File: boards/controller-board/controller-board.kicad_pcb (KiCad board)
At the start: 2 copper layers, 130 x 115 mm, 178 parts, among them J1 Conn_01x02, J2 Conn_01x02, J3 Conn_01x02, J4 Conn_01x02, J5 Conn_01x03, J6 Conn_01x02, Q1 SQS460EN, Q2 DGD0216, SW1 EG1271, U1 CAT4201, U10 CAT4201, U11 CAT4201, U12 CAT4201, U13 CAT4201, U14 CAT4201, U15 CAT4201, U17 CAT4201, U18 CAT4201, U2 PocketBeagle, U3 LTC3624, U4 CAT4201, U5 CAT4201, U6 CAT4201, U7 MCP4728, U8 ADS1015IRUGR, U9 ADS1015IRUGR

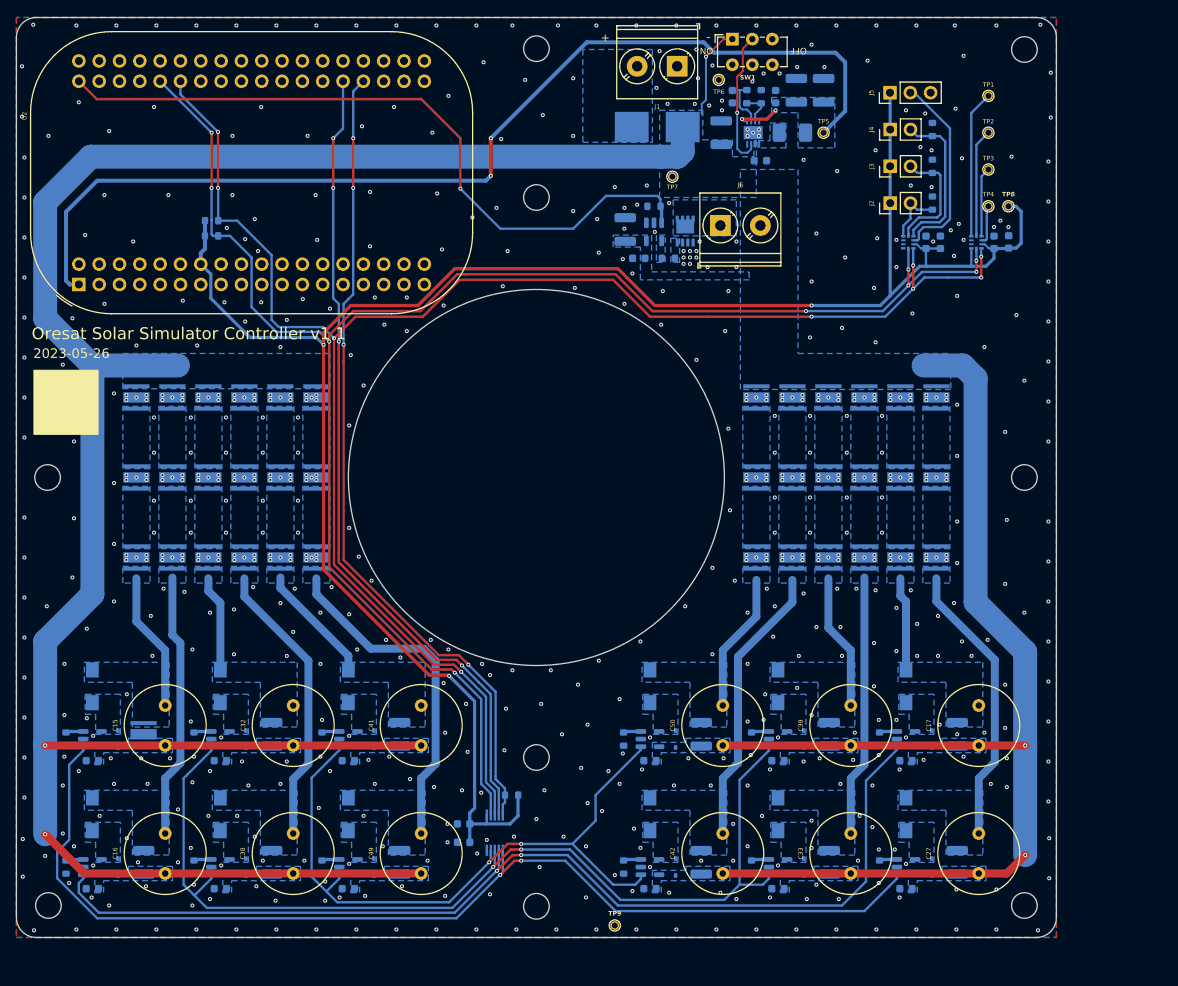
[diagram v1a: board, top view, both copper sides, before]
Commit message: moved LED driver circuitry to front layer of PCB
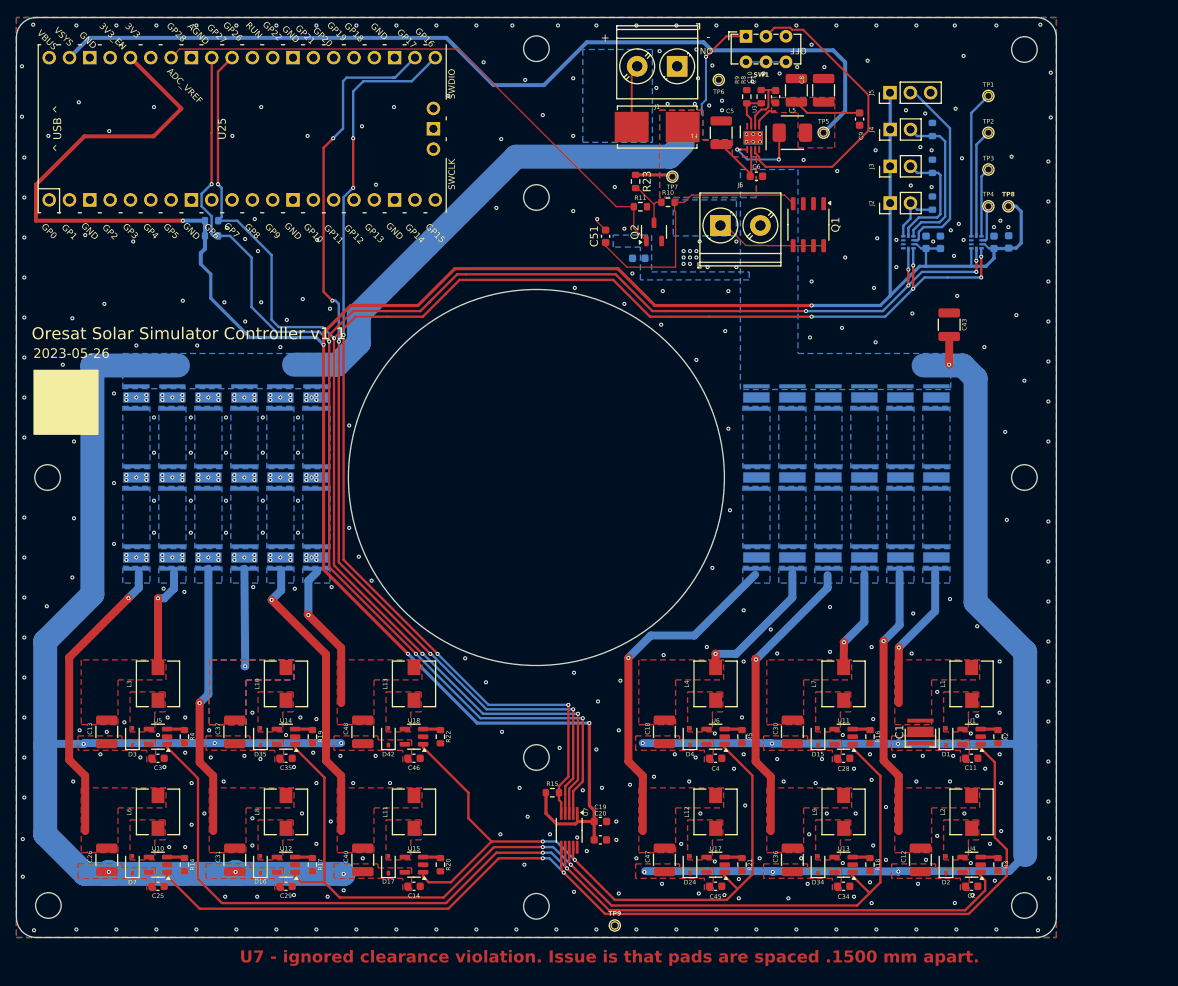
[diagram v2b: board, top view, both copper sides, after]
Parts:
- removed C15, C16, C17, C27, C32, C33, C38, C39, C41, C42, C49, C50: NP, Capacitor_THT:C_Radial_D10.0mm_H16.0mm_P5.00mm
- removed U2: PocketBeagle, Module:BeagleBoard_PocketBeagle
- added C51: C_Small, Capacitor_SMD:C_0603_1608Metric, F.Cu at (153.7, 72.3)
- added R23: 1k, Resistor_SMD:R_0603_1608Metric, F.Cu at (157.4, 65.5)
- added U25: RPi_Pico, oresat-misc:RPi_Pico_TH, F.Cu at (108.2, 58.9)
- C1, C10, C11, C12, C13, C14, C18, C19, C2, C20, C25, C26, C28, C29, C3, C30, C31, C34, C35, C36, C37, C4, C40, C43, C45, C46, C47, C48, C5, C6, C7, C8, C9, D1, D15, D16, D17, D2, D24, D3, D34, D35, D4, D42, D7, F1, L1, L10, L11, L12, L13, L2, L3, L4, L5, L6, L7, L8, L9, R10, R11, R14, R15, R16, R17, R18, R19, R2, R20, R21, R22, R3, R4, R5, R8, R9, U1, U10, U11, U12, U13, U14, U15, U17, U18, U4, U5, U6, U7: moved to F.Cu
- D18, D19, D20, D21: value XPEBBL-L1-0000-00201 -> ELUA3535OGB-P6070U23240500-VD1M
- D22, D23, D47, D48: value XPEBBL-L1-0000-00201 -> NP
- D43, D44, D45, D46: value XPEBBL-L1-0000-00201 -> ELUC3535NUB-P7085Q15070100-S22Q
- Q1: value SQS460EN -> Goford_G11S_20V_11A; footprint Package_SO:Vishay_PowerPAK_1212-8_Single -> Package_SO:SOP-8_3.9x4.9mm_P1.27mm; moved to F.Cu
- Q2: value DGD0216 -> PMV45EN; footprint Package_TO_SOT_SMD:TSOT-23-5 -> Package_TO_SOT_SMD:SOT-23-3; moved to F.Cu
- U3: footprint Package_DFN_QFN:DFN-8-1EP_3x3mm_P0.5mm_EP1.65x2.38mm -> oresat-ics:DFN-8-1EP_3x3mm_P0.5mm_EP1.65x2.38mm_ThermalVias0.3mm; moved to F.Cu
- moved R2 116.5 mm to (202.7, 134.9)
- moved R3 116.5 mm to (202.7, 150.9)
- moved C11 109.9 mm to (199.4, 137.6), turned to 0 degrees
- moved C2 109.9 mm to (199.4, 153.6), turned to 0 degrees
- moved L1 109.9 mm to (199.4, 128.3)
- moved L2 109.9 mm to (199.4, 144.3)
- moved U1 109.9 mm to (199.4, 134.9), turned to 180 degrees
- moved U4 109.9 mm to (199.4, 150.9), turned to 180 degrees
- moved C13 106.3 mm to (91.3, 134.3)
- moved C26 106.3 mm to (91.3, 150.3)
- moved D1 103.5 mm to (196.2, 134.9)
- moved D2 103.5 mm to (196.2, 150.9)
- moved D3 99.9 mm to (94.5, 134.9)
- moved D7 99.9 mm to (94.5, 150.9)
- moved C1 97.1 mm to (193.0, 134.3)
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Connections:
- C1 pad 2: Net-(D8-K) -> Net-(D26-K)
- C12 pad 2: Net-(D10-K) -> Net-(D12-K)
- C13 pad 2: Net-(D12-K) -> Net-(D10-K)
- C18 pad 2: Net-(D19-K) -> Net-(D21-K)
- C26 pad 2: Net-(D26-K) -> Net-(D8-K)
- C30 pad 2: Net-(D29-K) -> Net-(D31-K)
- C31 pad 2: Net-(D31-K) -> Net-(D29-K)
- C36 pad 2: Net-(D37-K) -> Net-(D39-K)
- C37 pad 2: Net-(D39-K) -> Net-(D37-K)
- C40 pad 2: Net-(D21-K) -> Net-(D19-K)
- C47 pad 2: Net-(D44-K) -> Net-(D46-K)
- C48 pad 2: Net-(D46-K) -> Net-(D44-K)
- L1 pad 2: Net-(D8-K) -> Net-(D26-K)
- L10 pad 2: Net-(D39-K) -> Net-(D37-K)
- L11 pad 2: Net-(D21-K) -> Net-(D19-K)
- L12 pad 2: Net-(D44-K) -> Net-(D46-K)
- L13 pad 2: Net-(D46-K) -> Net-(D44-K)
- L2 pad 2: Net-(D10-K) -> Net-(D12-K)
- L3 pad 2: Net-(D12-K) -> Net-(D10-K)
- L4 pad 2: Net-(D19-K) -> Net-(D21-K)
- L6 pad 2: Net-(D26-K) -> Net-(D8-K)
- L7 pad 2: Net-(D29-K) -> Net-(D31-K)
- L8 pad 2: Net-(D31-K) -> Net-(D29-K)
- L9 pad 2: Net-(D37-K) -> Net-(D39-K)
- Q2 pad 1: unconnected-(Q2-~{IN}-Pad1) -> Net-(Q2-G)
- Q2 pad 3: Net-(Q2-IN) -> Net-(Q2-D)
- R10 pad 1: Net-(Q2-OUT) -> Net-(Q2-D)
- R11 pad 1: Net-(Q2-IN) -> Net-(Q2-G)
- SW1 pad 4: (no net) -> GND
- SW1 pad 5: (no net) -> GND
- SW1 pad 6: (no net) -> GND
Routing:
- net Net-(Q2-IN): track 88.9 -> 0.00 mm, vias 1 -> 0
- net Net-(Q2-G): track 0.00 -> 71.9 mm
- net +3.3V: track 247.7 -> 317.2 mm, vias 3 -> 5
- net Net-(Q1-G): track 0.00 -> 34.1 mm
- net Net-(D46-K): track 17.4 -> 42.6 mm, vias 0 -> 1
- net Net-(D44-K): track 42.7 -> 18.7 mm, vias 0 -> 1
- net VCC: track 431.4 -> 407.6 mm, vias 5 -> 14
- net Net-(D37-K): track 36.0 -> 12.4 mm, vias 0 -> 1
- net Net-(D12-K): track 11.7 -> 33.9 mm, vias 0 -> 1
- net Net-(D29-K): track 12.1 -> 34.1 mm, vias 0 -> 1
- net Net-(D19-K): track 15.1 -> 36.5 mm, vias 0 -> 1
- net Net-(SW1-B): track 17.2 -> 38.6 mm, vias 1 -> 0
- net /DAC_~{LDAC}: track 102.3 -> 122.6 mm, vias 4 -> 5
- net Net-(D10-K): track 33.2 -> 13.2 mm, vias 0 -> 1
- net Net-(D31-K): track 32.7 -> 12.8 mm, vias 0 -> 1
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- added copper zone on F.Cu, net +5V
- added copper zone on F.Cu, net Net-(D1-A)
- added copper zone on F.Cu, net Net-(D10-K)
- added copper zone on F.Cu, net Net-(D12-K)
- added copper zone on F.Cu, net Net-(D15-A)
- added copper zone on F.Cu, net Net-(D16-A)
- added copper zone on F.Cu, net Net-(D17-A)
- added copper zone on F.Cu, net Net-(D19-K)
- added copper zone on F.Cu, net Net-(D2-A)
- added copper zone on F.Cu, net Net-(D21-K)
- added copper zone on F.Cu, net Net-(D24-A)
- added copper zone on F.Cu, net Net-(D26-K)
- added copper zone on F.Cu, net Net-(D29-K)
- added copper zone on F.Cu, net Net-(D3-A)
- added copper zone on F.Cu, net Net-(D31-K)
- added copper zone on F.Cu, net Net-(D34-A)
- added copper zone on F.Cu, net Net-(D35-A)
- added copper zone on F.Cu, net Net-(D37-K)
- added copper zone on F.Cu, net Net-(D39-K)
- added copper zone on F.Cu, net Net-(D4-A)
- added copper zone on F.Cu, net Net-(D42-A)
- added copper zone on F.Cu, net Net-(D44-K)
- added copper zone on F.Cu, net Net-(D46-K)
- added copper zone on F.Cu, net Net-(D7-A)
- added copper zone on F.Cu, net Net-(D8-K)
- added copper zone on F.Cu, net VCC
- removed copper zone on B.Cu, net +5V
- removed copper zone on B.Cu, net Net-(D1-A)
- removed copper zone on B.Cu, net Net-(D15-A)
- removed copper zone on B.Cu, net Net-(D16-A)
- removed copper zone on B.Cu, net Net-(D17-A)
- removed copper zone on B.Cu, net Net-(D2-A)
- removed copper zone on B.Cu, net Net-(D24-A)
- removed copper zone on B.Cu, net Net-(D3-A)
- removed copper zone on B.Cu, net Net-(D34-A)
- removed copper zone on B.Cu, net Net-(D35-A)
- removed copper zone on B.Cu, net Net-(D4-A)
- removed copper zone on B.Cu, net Net-(D42-A)
- removed copper zone on B.Cu, net Net-(D7-A)
- removed copper zone on B.Cu, net Net-(Q1-G)
- removed copper zone on B.Cu, net Net-(Q2-OUT)
- removed copper zone on B.Cu, net Net-(U3-SW)
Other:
- board text added: "U7 - ignored clearance violation. Issue is that pads are spaced .1500 mm apart."

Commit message: edited tracks in pcb
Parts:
- C21, C22, C23, C24, C44, R1, R12, R13, R6, R7, U8, U9: moved to F.Cu
- J2, J3, J4, J5, TP1, TP2, TP3, TP4, TP8: moved to B.Cu
- moved C22 15.7 mm to (188.4, 74.8)
- moved TP8 15.6 mm to (188.5, 70.3), turned to 180 degrees
- moved J5 14.2 mm to (203.3, 56.1)
- moved J2 14.1 mm to (203.3, 69.9)
- moved J3 14.1 mm to (203.3, 65.3)
- moved J4 14.1 mm to (203.3, 60.7)
- moved C21 12.0 mm to (190.3, 74.8)
- moved TP4 10.7 mm to (191.0, 70.3)
- moved TP1 10.7 mm to (191.0, 56.5)
- moved TP2 10.7 mm to (191.0, 61.1)
- moved TP3 10.7 mm to (191.0, 65.7)
- moved U8 9.64 mm to (201.0, 74.8), turned to 180 degrees
- moved C44 9.15 mm to (160.3, 66.3)
- moved U9 7.72 mm to (192.5, 74.8), turned to 180 degrees
- moved C43 7.32 mm to (189.9, 86.5)
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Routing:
- net +3.3V: track 317.2 -> 283.3 mm, vias 5 -> 3
- net +5V: track 125.3 -> 112.6 mm
- net Net-(D39-K): track 36.7 -> 49.2 mm
- net VCC: track 407.6 -> 396.9 mm, vias 14 -> 24
- net /SCL1: track 223.2 -> 219.5 mm, vias 9 -> 7
- net Net-(D31-K): track 12.8 -> 16.4 mm
- net Net-(D46-K): track 42.6 -> 39.4 mm
- net Net-(U3-SW): track 10.4 -> 7.42 mm
- net Net-(J6-Pin_1): track 14.0 -> 16.8 mm
- net Net-(D44-K): track 18.7 -> 21.6 mm
- net /SDA1: track 222.8 -> 220.1 mm, vias 9 -> 6
- net GND: track 6.81 -> 5.00 mm, vias 480 -> 455
- net /DAC_~{LDAC}: track 122.6 -> 121.4 mm, vias 5 -> 3
- net Net-(D19-K): track 36.5 -> 35.5 mm
- net Net-(D10-K): track 13.2 -> 14.0 mm
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
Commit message: added test points
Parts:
- added TP10: TestPoint-MinTH, oresat-misc:TestPoint-MinTH, F.Cu at (86.7, 74.5)
- added TP11: TestPoint-MinTH, oresat-misc:TestPoint-MinTH, F.Cu at (91.7, 74.5)
- added TP12: TestPoint-MinTH, oresat-misc:TestPoint-MinTH, F.Cu at (94.2, 74.5)
- added TP13: TestPoint-MinTH, oresat-misc:TestPoint-MinTH, F.Cu at (96.8, 74.5)
- TP8: moved to F.Cu
- moved TP8 104.4 mm to (84.2, 74.5), turned to 0 degrees
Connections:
- net Net-(Q2-G) renamed /PWM
- J6 pad 1: Net-(J6-Pin_1) -> GND
- J6 pad 2: VCC -> Net-(J6-Pin_2)
- Q1 pad 1: GND -> VCC
- Q1 pad 2: GND -> VCC
- Q1 pad 3: GND -> VCC
- Q1 pad 5: Net-(J6-Pin_1) -> Net-(J6-Pin_2)
- Q1 pad 6: Net-(J6-Pin_1) -> Net-(J6-Pin_2)
- Q1 pad 7: Net-(J6-Pin_1) -> Net-(J6-Pin_2)
- Q1 pad 8: Net-(J6-Pin_1) -> Net-(J6-Pin_2)
- TP8 pad 1: +3.3V -> Net-(U25-GPIO0)
- U25 pad 1: unconnected-(U25-GPIO0-Pad1) -> Net-(U25-GPIO0)
- U25 pad 2: unconnected-(U25-GPIO1-Pad2) -> Net-(U25-GPIO1)
- U25 pad 4: unconnected-(U25-GPIO2-Pad4) -> Net-(U25-GPIO2)
- U25 pad 5: unconnected-(U25-GPIO3-Pad5) -> Net-(U25-GPIO3)
- U25 pad 6: unconnected-(U25-GPIO4-Pad6) -> Net-(U25-GPIO4)
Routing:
- net Net-(J6-Pin_2): track 0.00 -> 26.6 mm
- net Net-(J6-Pin_1): track 16.8 -> 0.00 mm
- net VCC: track 396.9 -> 412.4 mm
- net +3.3V: track 283.3 -> 272.9 mm
- net Net-(U25-GPIO3): track 0.00 -> 7.35 mm
- net Net-(U25-GPIO0): track 0.00 -> 6.67 mm
- net Net-(U25-GPIO2): track 0.00 -> 6.66 mm
- net Net-(U25-GPIO1): track 0.00 -> 6.65 mm
- net Net-(U25-GPIO4): track 0.00 -> 6.65 mm
- net GND: track 5.00 -> 5.68 mm, vias 455 -> 453
- net +5V: track 112.6 -> 113.3 mm
- removed copper zone on B.Cu, net Net-(J6-Pin_1)

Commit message: minor pcb changes
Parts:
- J2, J3, J4, J5: moved to F.Cu
- moved R15 11.4 mm to (156.7, 147.8), turned to 90 degrees
- moved U7 6.74 mm to (152.4, 152.4)
- moved C19 5.65 mm to (155.9, 150.3)
- moved C20 5.35 mm to (155.2, 152.7), turned to -90 degrees
- turned J2 to -90 degrees
- turned J3 to -90 degrees
- turned J4 to -90 degrees
- turned J5 to -90 degrees
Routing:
- net /DAC_RDY/~{BSY}: track 120.8 -> 147.2 mm
- net /DAC_~{LDAC}: track 121.4 -> 127.9 mm
- net /SDA1: track 220.1 -> 226.5 mm
- net /SCL1: track 219.5 -> 225.8 mm
- net /RED_LIM: track 135.2 -> 130.6 mm
- net /GREEN_LIM: track 129.9 -> 127.2 mm
- net /BLUE_LIM: track 124.7 -> 122.5 mm
- net +3.3V: track 272.9 -> 271.1 mm
- net /UV_LIM: track 86.1 -> 84.5 mm
- net GND: vias 453 -> 476

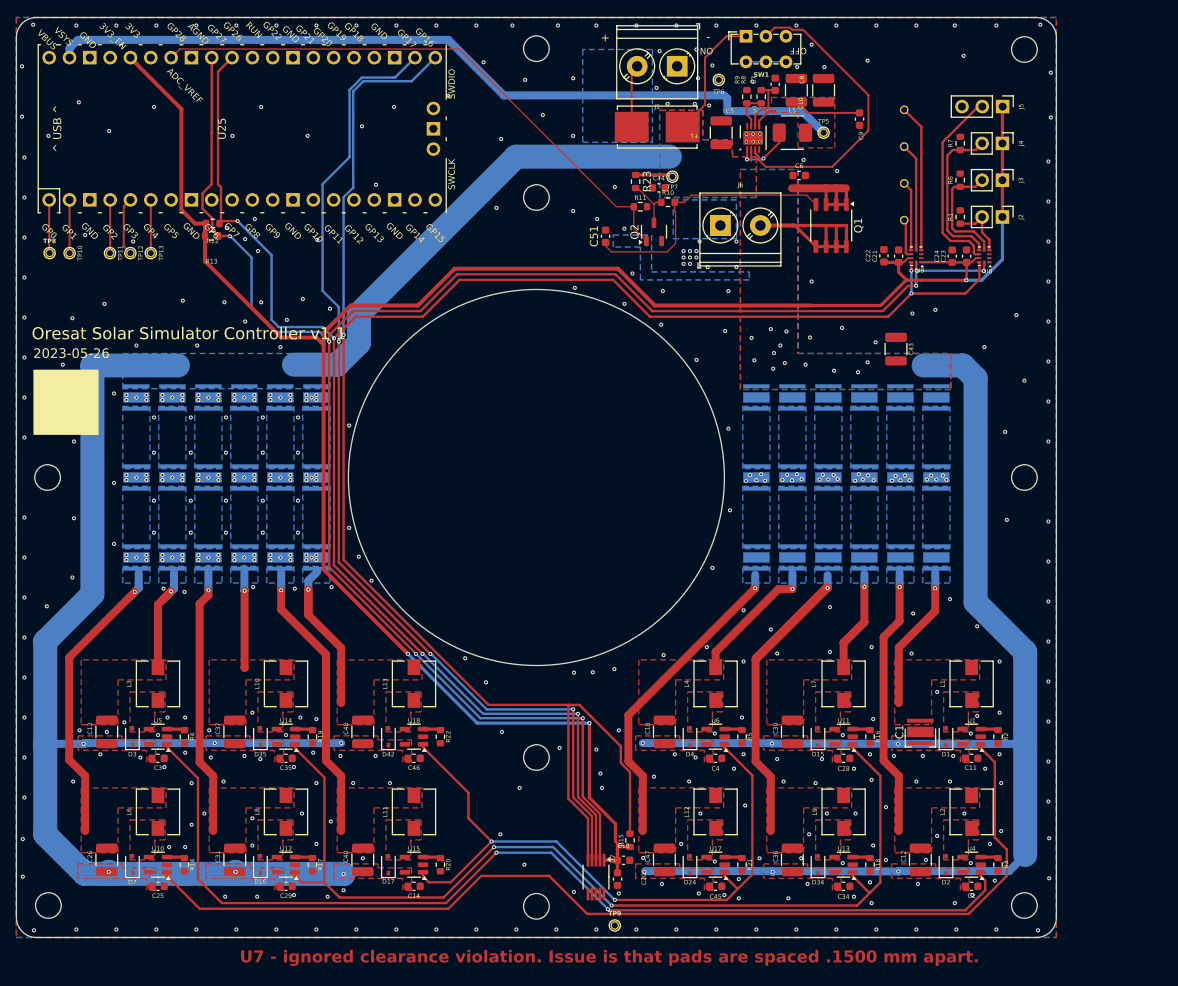
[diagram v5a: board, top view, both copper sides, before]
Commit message: added vias, changed ground pads to solid on some components, anadjusted tracks
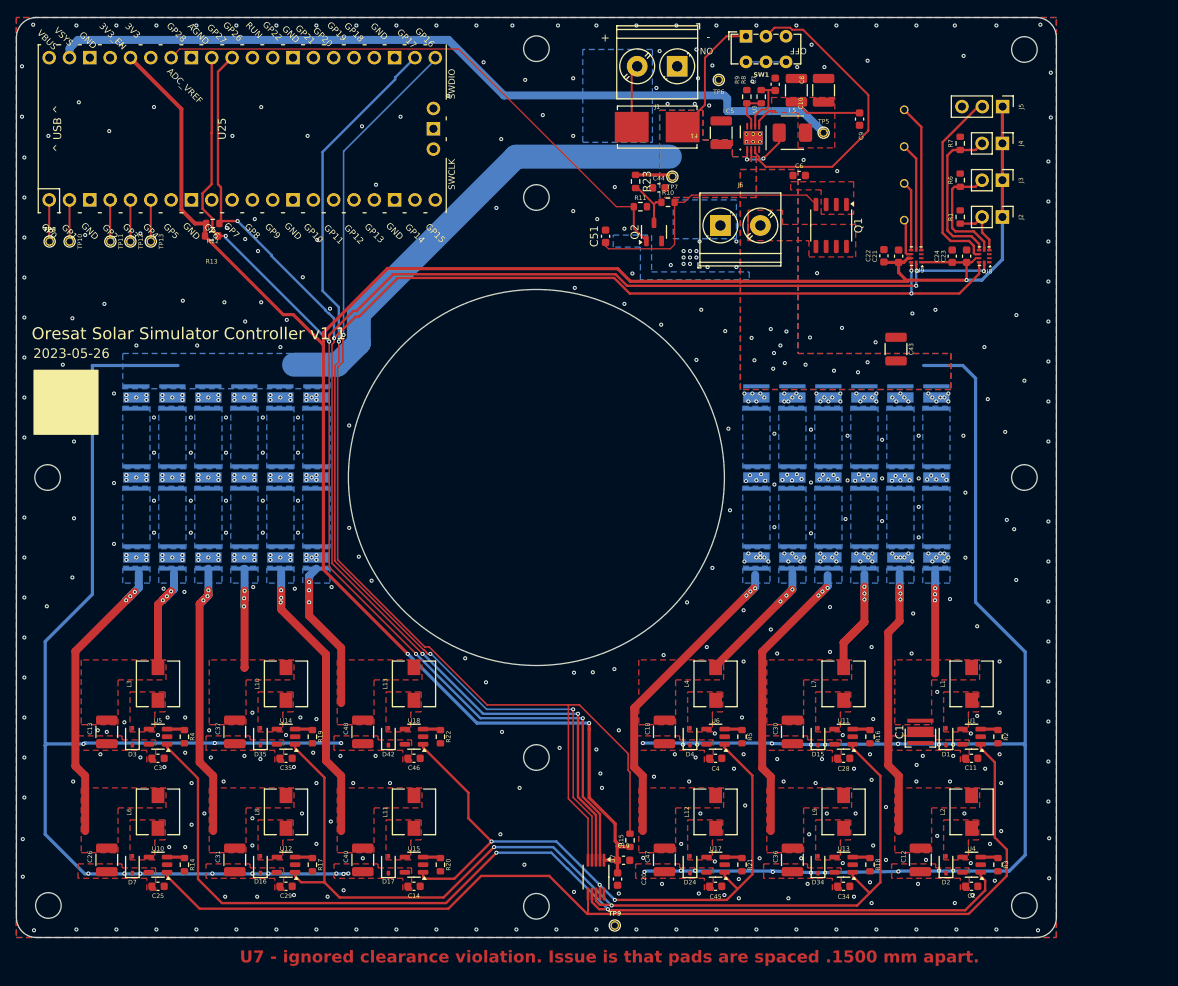
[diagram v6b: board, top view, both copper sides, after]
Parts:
- moved TP11 1.45 mm to (91.8, 73.0)
- moved TP10 1.45 mm to (86.7, 73.0)
- moved TP12 1.45 mm to (94.2, 73.0)
- moved TP13 1.45 mm to (96.8, 73.0)
- moved TP8 1.45 mm to (84.2, 73.0)
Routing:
- net Net-(J6-Pin_2): track 26.5 -> 0.14 mm
- net VCC: track 412.4 -> 398.4 mm, vias 24 -> 42
- net Net-(D39-K): track 49.2 -> 37.2 mm, vias 1 -> 3
- net /SCL1: track 225.8 -> 219.7 mm
- net /SDA1: track 226.5 -> 220.9 mm
- net +3.3V: track 271.1 -> 267.0 mm
- net Net-(D26-K): track 18.2 -> 14.3 mm, vias 1 -> 3
- net /GREEN_LIM: track 127.2 -> 130.6 mm
- net Net-(D10-K): track 14.0 -> 17.1 mm, vias 1 -> 3
- net /BLUE_LIM: track 122.5 -> 125.6 mm
- net /RED_LIM: track 130.6 -> 133.1 mm
- net Net-(D8-K): track 36.7 -> 39.1 mm, vias 1 -> 3
- net /DAC_RDY/~{BSY}: track 147.2 -> 144.9 mm
- net Net-(U25-GPIO3): track 7.35 -> 5.20 mm
- net Net-(D19-K): track 35.5 -> 37.5 mm, vias 1 -> 3
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- added copper zone on F.Cu, net Net-(J6-Pin_2)

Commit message: general changes
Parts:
- moved C20 1.03 mm to (155.9, 152.0), turned to 0 degrees
- moved R13 0.54 mm to (104.5, 72.8)
- moved U3 0.45 mm to (172.1, 59.6)
- moved R8 0.35 mm to (173.2, 54.5)
- moved R9 0.35 mm to (171.3, 54.5)
- moved R17 0.12 mm to (117.0, 150.8)
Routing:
- net Net-(D10-K): track 17.1 -> 11.7 mm, vias 3 -> 5
- net Net-(D44-K): track 21.4 -> 16.8 mm, vias 3 -> 5
- net Net-(D8-K): track 39.1 -> 35.2 mm, vias 3 -> 5
- net Net-(D21-K): track 18.6 -> 15.0 mm, vias 3 -> 5
- net Net-(D29-K): track 35.8 -> 32.7 mm, vias 3 -> 5
- net Net-(D37-K): track 14.3 -> 11.2 mm, vias 3 -> 5
- net Net-(D19-K): track 37.5 -> 34.5 mm, vias 3 -> 5
- net Net-(D31-K): track 18.0 -> 15.6 mm, vias 3 -> 5
- net Net-(D46-K): track 40.5 -> 38.2 mm, vias 3 -> 5
- net Net-(D26-K): track 14.3 -> 12.0 mm, vias 3 -> 5
- net /GREEN_LIM: track 130.6 -> 128.4 mm, vias 2 -> 0
- net Net-(D12-K): track 34.7 -> 32.8 mm, vias 3 -> 5
- net Net-(D39-K): track 37.2 -> 35.3 mm, vias 3 -> 5
- net Net-(Q1-G): track 33.2 -> 32.1 mm
- net /PHOTODIODE: track 24.3 -> 25.2 mm
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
